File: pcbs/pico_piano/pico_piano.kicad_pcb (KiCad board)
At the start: 2 copper layers, 73 x 47.5 mm, 22 parts, among them U1 Pico

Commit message: WIP: real hardware tests
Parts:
- ON/OFF1: moved to F.Cu
- moved ON/OFF1 49.5 mm to (105.0, 58.0), turned to 90 degrees
- moved DBG1 5.10 mm to (154.5, 62.5), turned to 0 degrees
- moved POWER1 5.06 mm to (124.0, 58.0), turned to 180 degrees
- moved 9V_BAT1 2.52 mm to (104.5, 64.5), turned to 0 degrees
- renumbered NOTE_A to NOTE_A1, NOTE_AIS to NOTE_AIS1, NOTE_B to NOTE_B1, NOTE_C to NOTE_C1, NOTE_CIS to NOTE_CIS1, NOTE_D to NOTE_D1, NOTE_DIS to NOTE_DIS1, NOTE_E to NOTE_E1, NOTE_F to NOTE_F1, NOTE_FIS to NOTE_FIS1, NOTE_G to NOTE_G1, NOTE_GIS to NOTE_GIS1
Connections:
- U1 pad 21: /GIS -> /B
- U1 pad 22: /A -> /AIS
- U1 pad 24: /AIS -> /A
- U1 pad 25: /B -> /GIS
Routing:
- net /FN3: track 0.00 -> 92.8 mm, vias 0 -> 2
- net /FN0: track 0.00 -> 92.6 mm, vias 0 -> 2
- net /FN1: track 0.00 -> 86.3 mm, vias 0 -> 2
- net /FN2: track 0.00 -> 85.8 mm, vias 0 -> 2
- net /3V3: track 0.00 -> 70.2 mm
- net /A: track 0.00 -> 60.0 mm
- net /GIS: track 0.00 -> 50.8 mm
- net /B: track 0.00 -> 47.9 mm
- net /E: track 0.00 -> 41.1 mm
- net /AIS: track 0.00 -> 39.4 mm
- net /F: track 0.00 -> 38.6 mm
- net /G: track 0.00 -> 38.4 mm
- net /SCK: track 0.00 -> 38.4 mm
- net /DIN: track 0.00 -> 38.3 mm, vias 0 -> 1
- net GND: track 0.00 -> 36.8 mm
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- added copper zone on B.Cu, net GND
- added copper zone on F.Cu, net GND
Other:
- board size 73 x 47.5 mm -> 73 x 48.2 mm
- board text added: "Pico Piano v0.1"

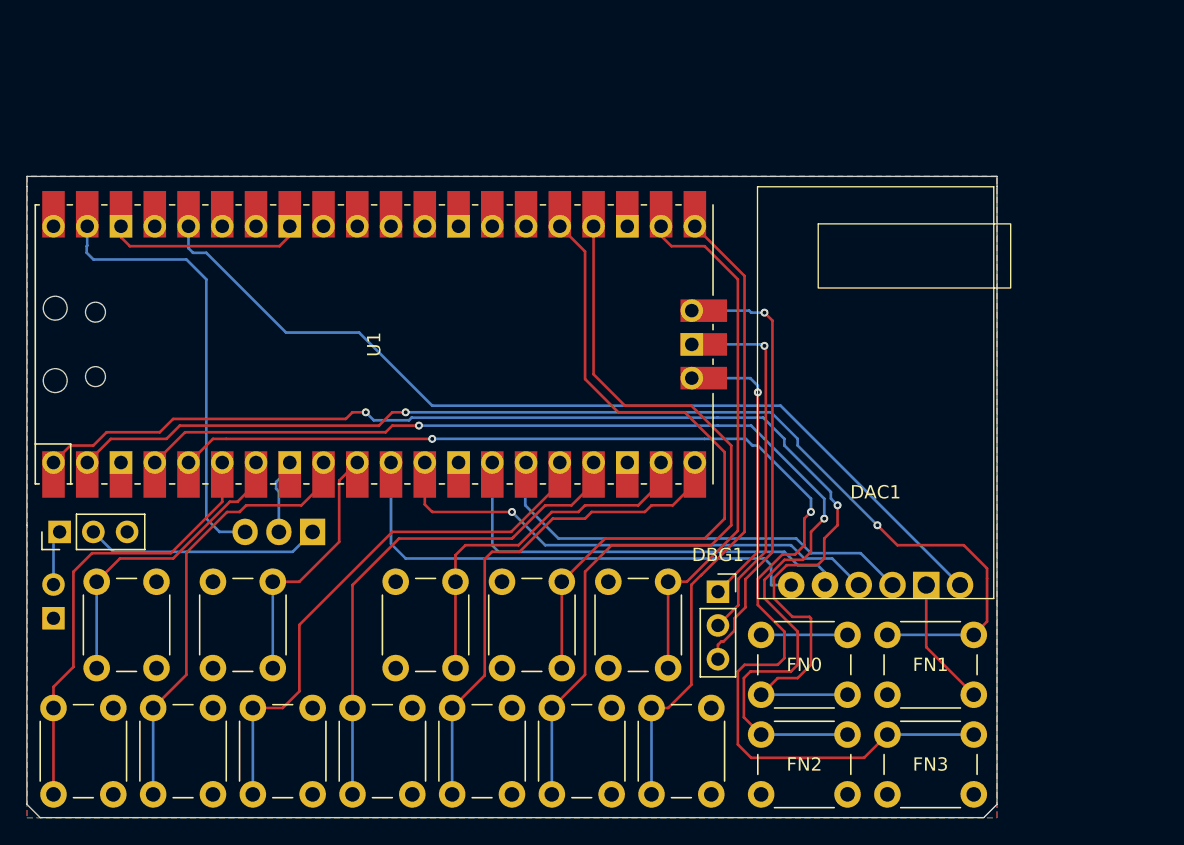
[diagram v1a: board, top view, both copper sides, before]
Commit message: Pico Piano PCB changes
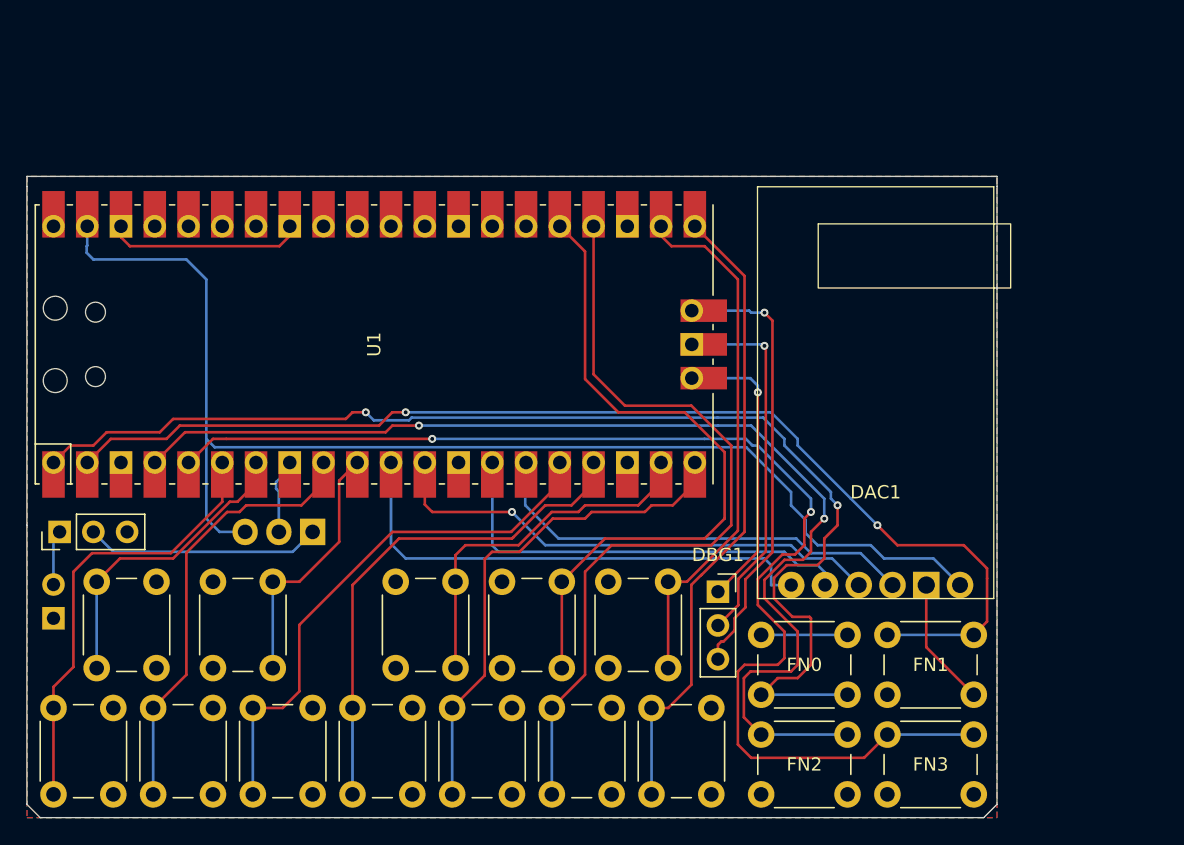
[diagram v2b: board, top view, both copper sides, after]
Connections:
- DAC1 pad 6: /3V3 -> +5V
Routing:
- net /3V3: track 70.2 -> 0.00 mm
- net +5V: track 33.2 -> 95.6 mm
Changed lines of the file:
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@@
 		(tags "Through hole socket strip THT 1x03 2.54mm single row")
 		(property "Reference" "DBG1"
-			(at 0 -2.77 360)
+			(at 0 -2.77 0)
 			(layer "F.SilkS")
 			(effects
@@
 		)
 		(property "Value" "Conn_01x03_Pin"
-			(at 0 7.85 360)
+			(at 0 7.85 0)
 			(layer "F.Fab")
 			(effects
@@
 			(layers "*.Cu" "*.Mask")
 			(remove_unused_layers no)
-			(net 6 "/3V3")
+			(net 24 "+5V")
 			(pinfunction "Pin_6")
 			(pintype "passive")
@@
 		)
 		(fp_text user "${REFERENCE}"
-			(at -3.5 0 270)
+			(at -3.5 0 -90)
 			(layer "B.Fab")
 			(hide yes)
@@
 	)
 	(segment
-		(start 159.215 48.5)
-		(end 133 48.5)
-		(width 0.2)
-		(layer "B.Cu")
-		(net 6)
-	)
-	(segment
-		(start 172.715 62)
-		(end 159.215 48.5)
-		(width 0.2)
-		(layer "B.Cu")
-		(net 6)
-	)
-	(segment
-		(start 114.66 36.66)
-		(end 114.66 35)
-		(width 0.2)
-		(layer "B.Cu")
-		(net 6)
-	)
-	(segment
-		(start 133 48.5)
-		(end 127.5 43)
-		(width 0.2)
-		(layer "B.Cu")
-		(net 6)
-	)
-	(segment
-		(start 116 37)
-		(end 115 37)
-		(width 0.2)
-		(layer "B.Cu")
-		(net 6)
-	)
-	(segment
-		(start 115 37)
-		(end 114.66 36.66)
-		(width 0.2)
-		(layer "B.Cu")
-		(net 6)
-	)
-	(segment
-		(start 127.5 43)
-		(end 122 43)
-		(width 0.2)
-		(layer "B.Cu")
-		(net 6)
-	)
-	(segment
-		(start 122 43)
-		(end 116 37)
-		(width 0.2)
-		(layer "B.Cu")
-		(net 6)
-	)
-	(segment
 		(start 132.44 55.94)
 		(end 132.44 52.78)
@@
 	)
 	(segment
-		(start 116 57)
-		(end 116 39)
+		(start 166 59)
+		(end 167 60)
+		(width 0.2)
+		(layer "B.Cu")
+		(net 24)
+	)
+	(segment
+		(start 167 60)
+		(end 170.715 60)
+		(width 0.2)
+		(layer "B.Cu")
+		(net 24)
+	)
+	(segment
+		(start 162 59)
+		(end 166 59)
+		(width 0.2)
+		(layer "B.Cu")
+		(net 24)
+	)
+	(segment
+		(start 161.1 57.1)
+		(end 161.1 58.1)
+		(width 0.2)
+		(layer "B.Cu")
+		(net 24)
+	)
+	(segment
+		(start 160 55)
+		(end 160 56)
 		(width 0.2)
 		(layer "B.Cu")
@@
 	)
 	(segment
+		(start 116 51)
+		(end 116 39)
+		(width 0.2)
+		(layer "B.Cu")
+		(net 24)
+	)
+	(segment
 		(start 107.04 36.46)
 		(end 107.04 35)
@@
 	)
 	(segment
+		(start 116 51)
+		(end 116.63 51.63)
+		(width 0.2)
+		(layer "B.Cu")
+		(net 24)
+	)
+	(segment
 		(start 118.92 58)
 		(end 117 58)
@@
 	)
 	(segment
+		(start 116.63 51.63)
+		(end 156.63 51.63)
+		(width 0.2)
+		(layer "B.Cu")
+		(net 24)
+	)
+	(segment
+		(start 161.1 58.1)
+		(end 162 59)
+		(width 0.2)
+		(layer "B.Cu")
+		(net 24)
+	)
+	(segment
+		(start 156.63 51.63)
+		(end 160 55)
+		(width 0.2)
+		(layer "B.Cu")
+		(net 24)
+	)
+	(segment
+		(start 160 56)
+		(end 161.1 57.1)
+		(width 0.2)
+		(layer "B.Cu")
+		(net 24)
+	)
+	(segment
 		(start 107 37)
 		(end 107 36.5)
@@
 		(width 0.2)
 		(layer "B.Cu")
+		(net 24)
+	)
+	(segment
+		(start 170.715 60)
+		(end 172.715 62)
+		(width 0.2)
+		(layer "B.Cu")
+		(net 24)
+	)
+	(segment
+		(start 116 57)
+		(end 116 51)
+		(width 0.2)
+		(layer "B.Cu")

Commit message: Update pico piano PCB
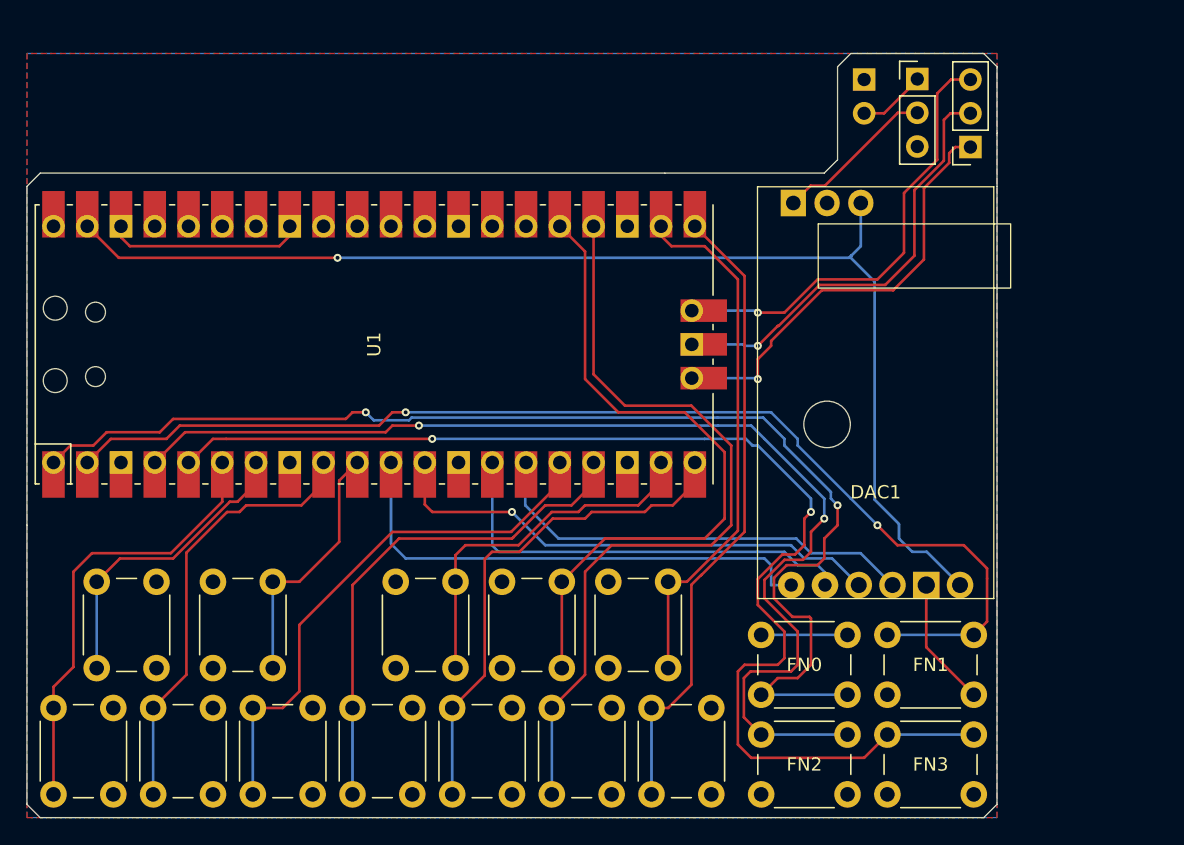
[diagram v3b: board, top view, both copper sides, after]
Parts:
- POWER1: footprint Package_TO_SOT_THT:TO-220-3_Vertical -> Package_TO_SOT_THT:TO-220-3_Horizontal_TabDown
- moved 9V_BAT1 73.2 mm to (165.5, 24.0), turned to 180 degrees
- moved ON/OFF1 73.0 mm to (169.5, 23.9), turned to 0 degrees
- moved POWER1 43.8 mm to (160.2, 33.2), turned to 0 degrees
- moved DBG1 38.5 mm to (173.5, 29.0), turned to 180 degrees
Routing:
- net Net-(DBG1-Pin_1): track 21.9 -> 32.9 mm
- net GND: track 36.8 -> 31.1 mm
- net Net-(POWER1-VI): track 17.7 -> 12.1 mm
- net Net-(DBG1-Pin_2): track 28.1 -> 33.0 mm
- net +5V: track 95.6 -> 91.7 mm, vias 0 -> 1
- net +9V: track 4.15 -> 5.12 mm
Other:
- board size 73 x 48.2 mm -> 73 x 57.5 mm

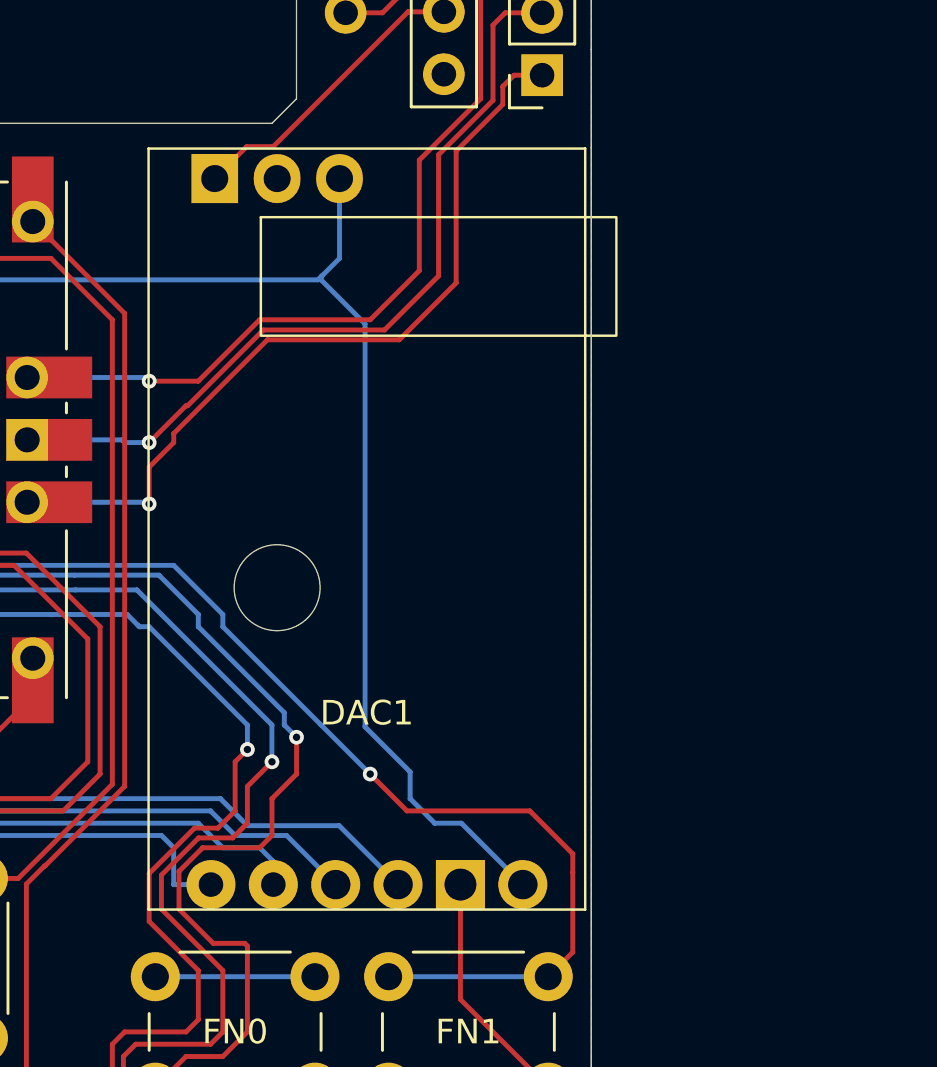
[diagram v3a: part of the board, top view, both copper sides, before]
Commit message: Add attack function
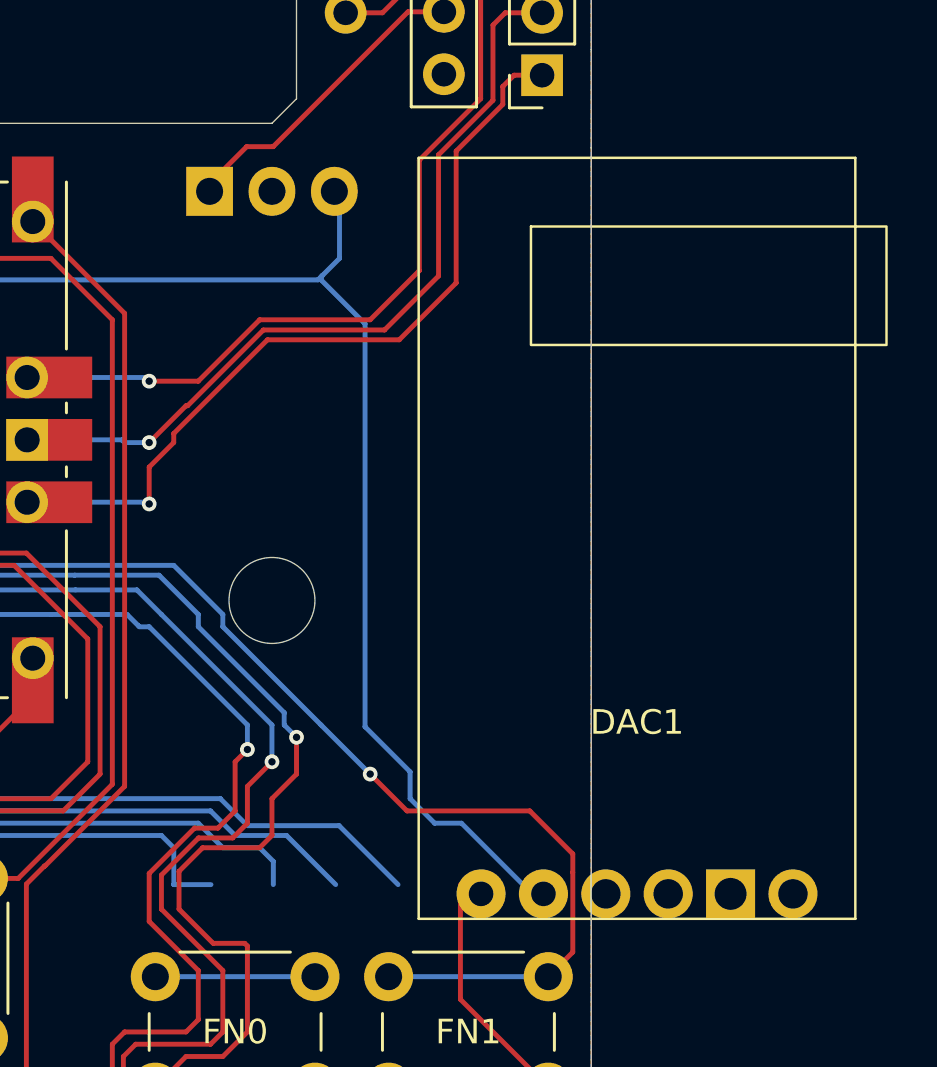
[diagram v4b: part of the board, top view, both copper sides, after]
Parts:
- moved DAC1 11.0 mm to (177.4, 63.4)
- moved POWER1 0.56 mm to (160.0, 33.8)
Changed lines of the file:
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@@
 		(tags "Through hole socket strip THT 1x03 2.54mm single row")
 		(property "Reference" "DBG1"
-			(at 0 -2.77 360)
+			(at 0 -2.77 0)
 			(layer "F.SilkS")
 			(hide yes)
@@
 		)
 		(property "Value" "Conn_01x03_Pin"
-			(at 0 7.85 360)
+			(at 0 7.85 0)
 			(layer "F.Fab")
 			(effects
@@
 	(footprint "rytmos:PCM5102_BREAKOUT"
 		(layer "F.Cu")
-		(at 166.365 63.016)
+		(at 177.365 63.394)
 		(property "Reference" "DAC1"
 			(at 0 -8 0)
@@
 	(footprint "Package_TO_SOT_THT:TO-220-3_Horizontal_TabDown"
 		(layer "B.Cu")
-		(at 160.17 33.25)
+		(at 159.96 33.77)
 		(descr "TO-220-3, Horizontal, RM 2.54mm, see https://www.vishay.com/docs/66542/to-220-1.pdf")
 		(tags "TO-220-3 Horizontal RM 2.54mm")
